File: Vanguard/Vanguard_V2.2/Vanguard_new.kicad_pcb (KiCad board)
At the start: 4 copper layers, 46.2 x 50.9 mm, 74 parts, among them J1 USB_C, J2 Conn_02x03_Pin, J3 Micro_SD_Card_Det1, J4 STARBOARD_SERVO, J5 PORTSIDE_SERVO, J6 Conn_01x02_Pin, Q1 BSS138, Q2 BSS138, Q3 BSS138, Q4 BSS138, U1 ATSAMD11D14A-M, U2 ATmega4809-A, U3 AT25DF641A-SH-T, U4 AP2112K-3.3, U5 MPM3610AGQV-P, U6 BNO086, U7 TXB0104D, U8 TPS61092, Y1 32.768kHz

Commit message: PCB
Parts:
- removed REF** (x3): MountingHole_2.2mm_M2, MountingHole:MountingHole_2.2mm_M2
- moved J3 310.8 mm to (424.9, 88.1), turned to 180 degrees
- moved D6 302.1 mm to (429.7, 64.5), turned to 90 degrees
- moved U5 300.3 mm to (428.0, 59.9)
- moved R14 300.0 mm to (423.9, 61.1), turned to 0 degrees
- moved C4 299.5 mm to (423.7, 60.2), turned to 180 degrees
- moved U7 299.1 mm to (425.1, 98.4), turned to 90 degrees
- moved J2 295.7 mm to (406.3, 71.4), turned to 180 degrees
- moved D1 294.8 mm to (398.5, 61.8), turned to 90 degrees
- moved J1 294.3 mm to (394.0, 62.0), turned to -90 degrees
- moved R15 294.0 mm to (427.0, 63.2)
- moved C5 292.4 mm to (427.2, 64.2), turned to 180 degrees
- moved R16 291.9 mm to (425.1, 63.2), turned to 180 degrees
- moved J5 290.2 mm to (398.9, 100.9), turned to -90 degrees
- moved R2 290.0 mm to (399.9, 65.2), turned to 180 degrees
- moved R1 289.8 mm to (396.0, 62.9)
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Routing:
- net RST: track 184.1 -> 40.0 mm, vias 13 -> 1
- net GND: track 88.2 -> 181.6 mm, vias 28 -> 19
- net VBUS_out: track 83.5 -> 16.7 mm, vias 6 -> 0
- net +5V: track 65.7 -> 16.0 mm, vias 2 -> 0
- net SDA: track 40.7 -> 10.2 mm, vias 3 -> 0
- net PORT_SERVO: track 27.5 -> 0.00 mm, vias 1 -> 0
- net STAR_SERVO: track 27.3 -> 0.00 mm, vias 1 -> 0
- net PA1/MOSI: track 20.8 -> 0.00 mm, vias 2 -> 0
- net PA2/SCK: track 19.1 -> 0.00 mm, vias 2 -> 0
- net UPDI: track 39.0 -> 20.7 mm, vias 4 -> 0
- net (no net): track 0.00 -> 17.3 mm
- net D7: track 16.1 -> 0.00 mm, vias 2 -> 0
- net D4: track 15.4 -> 0.00 mm, vias 2 -> 0
- net D6: track 15.0 -> 0.00 mm
- net Net-(J2-Pin_6): track 19.0 -> 4.00 mm, vias 3 -> 0
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- added copper zone on B.Cu, net (none)
- added copper zone on F.Cu, net (none)
- added copper zone on In1.Cu, net GND
- added copper zone on In2.Cu, net GND
- removed copper zone on B.Cu, net GND
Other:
- board size 46.2 x 50.9 mm -> 420.8 x 192.8 mm
- board text removed: "portside"
- board text removed: "starboard"

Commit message: started pcb
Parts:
- removed J1: USB_C, Connector_USB:USB_C_Plug_Molex_105444
- added J7: USB_B_Micro, Connector_USB:USB_Micro-B_Wuerth_614105150721_Vertical_CircularHoles, F.Cu at (108.3, 39.6)
- moved U7 398.0 mm to (35.6, 180.2), turned to 180 degrees
- moved J3 389.6 mm to (45.8, 178.2), turned to 90 degrees
- moved R22 373.4 mm to (25.6, 107.3)
- moved R23 371.4 mm to (29.2, 107.5), turned to 0 degrees
- moved R21 370.4 mm to (27.6, 107.3)
- moved Y1 370.3 mm to (26.6, 111.9), turned to -90 degrees
- moved C2 368.6 mm to (28.0, 110.7)
- moved ADR1 368.3 mm to (32.4, 106.7), turned to 180 degrees
- moved C3 368.1 mm to (28.0, 114.9), turned to -90 degrees
- moved U6 366.2 mm to (30.5, 111.7), turned to 90 degrees
- moved R20 366.1 mm to (33.7, 108.4), turned to 0 degrees
- moved R19 365.6 mm to (33.2, 110.0)
- moved R18 363.2 mm to (33.7, 111.5), turned to 0 degrees
- moved R24 362.9 mm to (30.8, 115.6), turned to 90 degrees
- moved C7 362.4 mm to (33.4, 112.5), turned to 0 degrees
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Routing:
- net GND: track 181.6 -> 6.33 mm, vias 19 -> 0
- net UPDI: track 20.7 -> 0.00 mm
- net RST: track 40.0 -> 19.7 mm, vias 1 -> 0
- net Net-(D1-I/O1): track 19.8 -> 0.00 mm
- net Net-(D1-I/O2): track 18.0 -> 0.00 mm, vias 2 -> 0
- net (no net): track 17.3 -> 0.00 mm
- net Net-(D2-K): track 17.0 -> 0.00 mm
- net Net-(D3-K): track 16.2 -> 0.00 mm
- net Net-(J2-Pin_2): track 13.4 -> 0.00 mm, vias 2 -> 0
- net RX0: track 12.5 -> 0.00 mm
- net TX0: track 12.4 -> 0.00 mm, vias 2 -> 0
- net SCL: track 12.0 -> 0.00 mm, vias 2 -> 0
- net +5V: track 16.0 -> 4.63 mm
- net Net-(J2-Pin_3): track 11.1 -> 0.00 mm
- net SDA: track 10.2 -> 0.00 mm
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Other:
- board size 420.8 x 192.8 mm -> 277.3 x 192.8 mm

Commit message: schematic + pcb changes
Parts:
- removed U5: MPM3610AGQV-P, MPM3610AGQV_P:CONV_MPM3620AGQV-P
- added U9: MPM3610AGQV-P, MPM3610AGQV_P:CONV_MPM3620AGQV-P, F.Cu at (278.9, 26.6)
- moved C5 78.7 mm to (282.3, 26.1), turned to 90 degrees
- moved C6 77.0 mm to (284.1, 26.7), turned to 180 degrees
- moved R15 45.3 mm to (281.4, 25.9), turned to 90 degrees
- moved D5 44.0 mm to (283.7, 24.9), turned to 180 degrees
- moved R17 33.9 mm to (283.9, 25.8), turned to 180 degrees
- moved R16 31.6 mm to (281.5, 24.0), turned to 90 degrees
- moved U4 3.32 mm to (283.2, 28.8)
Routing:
- net Net-(U9-FB): track 0.00 -> 11.1 mm
- net Net-(U4-EN): track 0.00 -> 7.61 mm
- net Net-(D5-A): track 0.00 -> 0.87 mm
- net RST: track 19.7 -> 20.6 mm

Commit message: pcb finished
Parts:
- removed J7: USB_B_Micro, Connector_USB:USB_Micro-B_Wuerth_614105150721_Vertical_CircularHoles
- removed R8: DNP, Resistor_SMD:R_0402_1005Metric
- added P1: USB_C_Plug_USB2.0, Connector_USB:USB_C_Plug_Molex_105444, F.Cu at (340.5, 83.7)
- moved U7 337.8 mm to (363.0, 97.1), turned to 90 degrees
- moved J3 326.9 mm to (365.0, 107.4), turned to 0 degrees
- moved R22 314.8 mm to (340.2, 94.7)
- moved C7 314.1 mm to (347.3, 100.0)
- moved ADR1 314.1 mm to (346.3, 94.0)
- moved C2 314.1 mm to (341.9, 98.1)
- moved C3 314.1 mm to (341.9, 102.2)
- moved R18 314.1 mm to (347.5, 98.8)
- moved R19 314.1 mm to (347.1, 97.3)
- moved R21 314.1 mm to (341.5, 94.6)
- moved Y1 314.1 mm to (340.5, 99.2)
- moved R20 314.1 mm to (347.5, 95.8)
- moved R23 314.1 mm to (343.1, 94.8)
- moved R24 314.1 mm to (344.6, 102.9)
- moved U6 314.1 mm to (344.4, 99.1)
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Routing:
- net RST: track 20.6 -> 194.7 mm, vias 0 -> 16
- net GND: track 6.33 -> 111.6 mm, vias 0 -> 25
- net +5V: track 4.63 -> 86.0 mm, vias 0 -> 1
- net VBUS_out: track 10.5 -> 76.9 mm, vias 0 -> 3
- net PORT_SERVO: track 0.00 -> 51.6 mm, vias 0 -> 1
- net PORT_BLUE: track 0.00 -> 50.4 mm, vias 0 -> 2
- net PORT_GREEN: track 0.00 -> 50.3 mm, vias 0 -> 2
- net PORT_RED: track 0.00 -> 49.1 mm, vias 0 -> 2
- net STAR_SERVO: track 0.00 -> 45.6 mm, vias 0 -> 1
- net SCL: track 0.00 -> 43.7 mm, vias 0 -> 2
- net UPDI: track 0.00 -> 40.2 mm, vias 0 -> 2
- net SDA: track 0.00 -> 35.5 mm, vias 0 -> 2
- net CD: track 0.00 -> 32.8 mm, vias 0 -> 2
- net STAR_BLUE: track 0.00 -> 31.9 mm
- net D4: track 0.00 -> 31.0 mm, vias 0 -> 4
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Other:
- board size 277.3 x 192.8 mm -> 377.4 x 192.8 mm
- board text added: "PCB Edge"

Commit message: pcb changes
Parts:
- moved C6 165.6 mm to (218.8, 91.5)
- moved C8 165.6 mm to (193.4, 93.0)
- moved D3 165.6 mm to (193.9, 106.4)
- moved D6 165.6 mm to (217.8, 101.2)
- moved R3 165.6 mm to (195.6, 106.4)
- moved R4 165.6 mm to (195.0, 97.5)
- moved STARBOARD_RGB1 165.6 mm to (220.0, 127.3)
- moved BZ1 165.6 mm to (218.3, 119.0)
- moved C10 165.6 mm to (202.7, 93.9)
- moved C2 165.6 mm to (177.0, 113.3)
- moved C3 165.6 mm to (177.0, 117.5)
- moved C4 165.6 mm to (214.9, 96.9)
- moved C5 165.6 mm to (218.2, 93.2)
- moved C7 165.6 mm to (182.4, 115.2)
- moved C9 165.6 mm to (203.5, 93.8)
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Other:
- board size 377.4 x 192.8 mm -> 50 x 40 mm

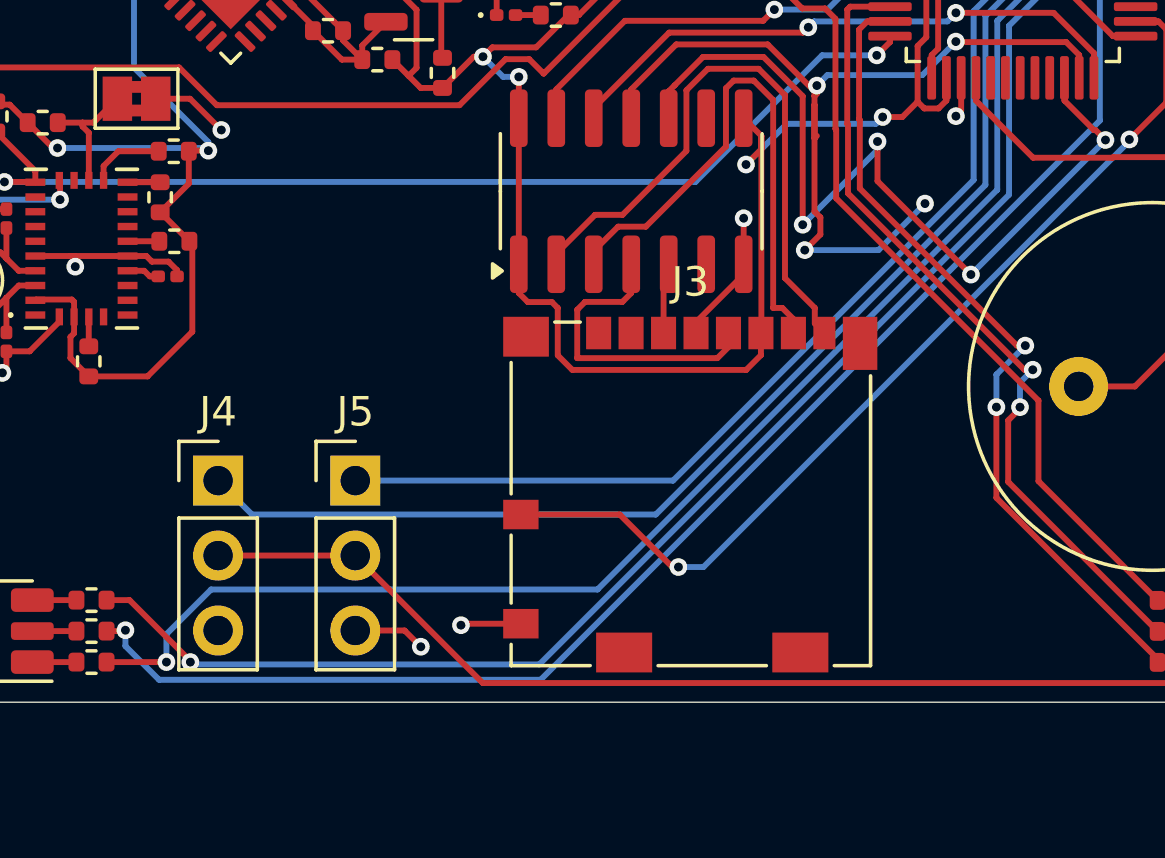
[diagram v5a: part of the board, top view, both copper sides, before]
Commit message: port side starboard servo port swap
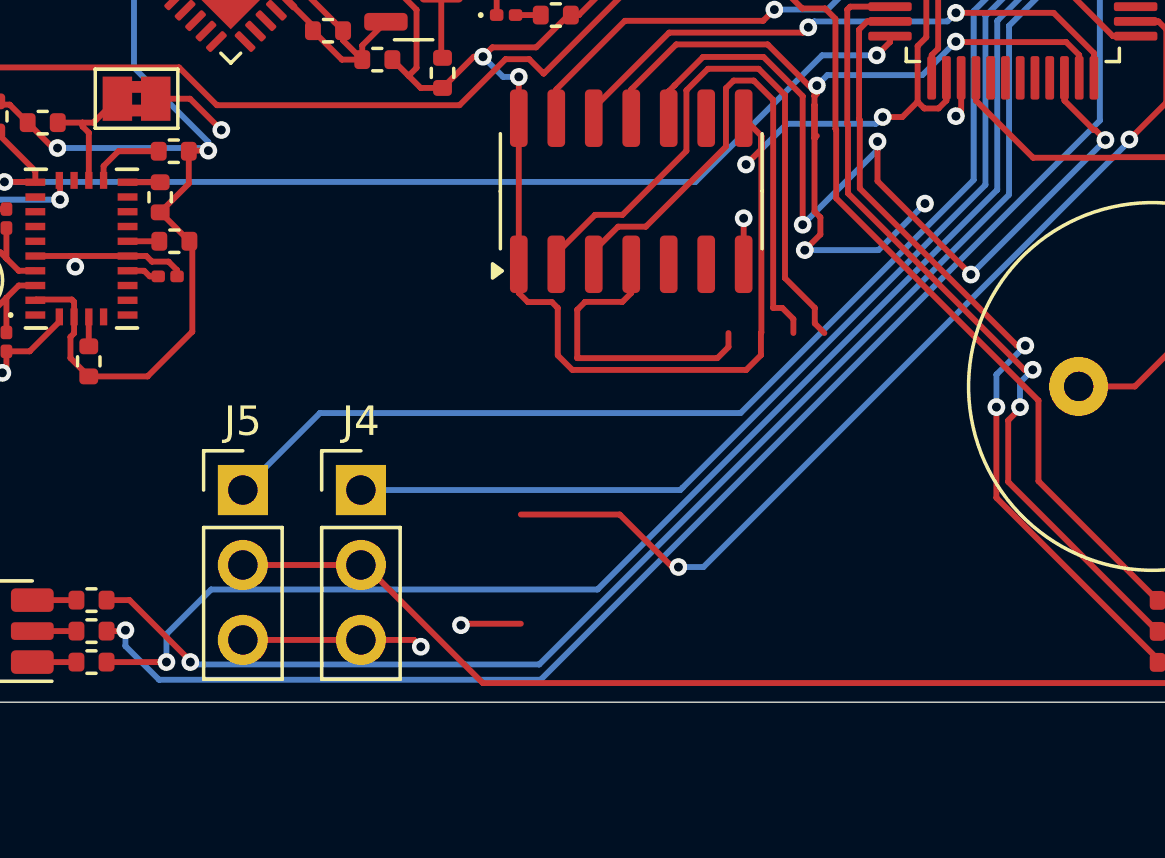
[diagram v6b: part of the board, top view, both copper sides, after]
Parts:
- removed J3: Micro_SD_Card_Det1, Connector_Card:microSD_HC_Molex_104031-0811
- moved J4 4.85 mm to (189.0, 122.5)
- moved J5 3.82 mm to (185.0, 122.5)
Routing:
- net STAR_SERVO: track 45.6 -> 40.0 mm
- net PORT_SERVO: track 51.6 -> 55.5 mm
- net Net-(J3-CMD): track 2.40 -> 0.25 mm
- net GND: track 111.6 -> 112.6 mm
- net +5V: track 86.0 -> 85.3 mm

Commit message: started wiring pcb
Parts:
- removed P1: USB_C_Plug_USB2.0, Connector_USB:USB_C_Plug_Molex_105444
- added J1: USB_C_Receptacle_USB2.0_16P, Connector_USB:USB_C_Receptacle_Amphenol_12401548E4-2A, F.Cu at (48.2, 24.9)
- added J3: Micro_SD_Card_Det1, Connector_Card:microSD_HC_Molex_104031-0811, F.Cu at (55.1, 158.9)
- added R31: 5k1, Resistor_SMD:R_0402_1005Metric, F.Cu at (70.8, 37.2)
- added R32: 5k1, Resistor_SMD:R_0402_1005Metric, F.Cu at (70.8, 39.2)
- added R8: DNP, Resistor_SMD:R_0402_1005Metric, F.Cu at (62.1, 33.3)
- added U5: BD1020HFV, Package_TO_SOT_SMD:HVSOF5, F.Cu at (75.7, 112.1)
- C10: value 100 uF -> 100u; footprint Capacitor_SMD:C_0201_0603Metric -> Capacitor_SMD:CP_Elec_6.3x5.4
- C2, C3: value 22pF -> 2p2
- C7: value 0.1uF -> 0u1F
- C8: value 10 uF -> 10u
- C9: value 2.2uF -> 2u2
- L1: value 6.8 uH -> 6u8
- R19, R20: value 4.7k -> 4k7
- R21, R22: value 2.2k -> 2k2
- U3: footprint AT25DF641A-SH-T:SOIC127P798X216-8N -> Package_SO:SOIC-8_3.9x4.9mm_P1.27mm
- U6: footprint BNO086:IC_BNO086 -> Package_LGA:LGA-28_5.2x3.8mm_P0.5mm
- U9: footprint MPM3610AGQV_P:CONV_MPM3620AGQV-P -> Package_DFN_QFN:QFN-16-1EP_3x3mm_P0.5mm_EP1.7x1.7mm
- moved U7 159.9 mm to (44.8, 157.6), turned to 0 degrees
- moved R3 152.9 mm to (59.2, 37.2), turned to 0 degrees
- moved R7 150.8 mm to (62.1, 31.3), turned to 0 degrees
- moved R10 148.4 mm to (62.1, 37.2), turned to 0 degrees
- moved R4 147.7 mm to (59.2, 39.2), turned to 0 degrees
- moved R13 147.6 mm to (62.1, 43.2)
- moved R6 145.5 mm to (59.2, 43.2), turned to 0 degrees
- moved R9 144.6 mm to (62.1, 35.3), turned to 0 degrees
- moved R5 144.5 mm to (59.2, 41.2)
- moved R12 143.8 mm to (62.1, 41.2)
- moved Q2 141.5 mm to (74.9, 32.6)
- moved R2 140.5 mm to (59.2, 35.3), turned to 0 degrees
- moved Q1 139.5 mm to (74.9, 28.0)
- moved R11 138.6 mm to (62.1, 39.2), turned to 0 degrees
- moved R1 137.3 mm to (59.2, 33.3)
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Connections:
- net RST renamed +3.3V
- C1 pad 1: VBUS_out -> Net-(D1-GND)
- C5 pad 1: Net-(U4-EN) -> Net-(D6-K)
- C8 pad 1: VBUS_out -> Net-(D1-GND)
- D1 pad 1: VBUS_out -> Net-(D1-GND)
- D1 pad 4: VBUS_out -> Net-(D1-GND)
- D6 pad 1: GND -> Net-(D6-K)
- D6 pad 2: VBUS_out -> Net-(D1-GND)
- J6 pad 1: VBUS_out -> Net-(D1-GND)
- L1 pad 1: VBUS_out -> Net-(D1-GND)
- Q1 pad 2: /RX_UPDI -> /TX_UPDI
- R1 pad 1: VBUS_out -> Net-(D1-GND)
- R15 pad 1: Net-(U4-EN) -> Net-(D6-K)
- R5 pad 2: /RX_UPDI -> /TX_UPDI
- R6 pad 2: /RX_UPDI -> /TX_UPDI
- U1 pad 11: /RX_UPDI -> /TX_UPDI
- U1 pad 15: Net-(D3-K) -> Net-(D2-K)
- U1 pad 16: Net-(D2-K) -> Net-(D3-K)
- U2 pad 3: unconnected-(U2-PA7-Pad3) -> TEMP_SENSOR
- U4 pad 1: Net-(U4-EN) -> Net-(D6-K)
- U4 pad 3: Net-(U4-EN) -> Net-(D6-K)
- U8 pad 11: VBUS_out -> Net-(D1-GND)
- U8 pad 8: VBUS_out -> Net-(D1-GND)
- U9 pad 2: VBUS_out -> unconnected-(U9-VCC-Pad2)
- U9 pad 4: Net-(U9-SW-Pad19) -> unconnected-(U9-SW-Pad19)_1
- U9 pad 5: Net-(U9-SW-Pad19) -> unconnected-(U9-SW-Pad19)_2
- U9 pad 6: Net-(U9-SW-Pad19) -> unconnected-(U9-SW-Pad19)
- U9 pad 7: Net-(U4-EN) -> Net-(D6-K)
- U9 pad 8: Net-(U4-EN) -> Net-(D6-K)
- U9 pad 9: Net-(U4-EN) -> Net-(D6-K)
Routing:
- net +3.3V: track 194.7 -> 17.3 mm, vias 16 -> 0
- net +5V: track 85.3 -> 0.00 mm, vias 1 -> 0
- net GND: track 112.6 -> 33.7 mm, vias 25 -> 0
- net VBUS_out: track 76.9 -> 0.00 mm, vias 3 -> 0
- net PORT_SERVO: track 55.5 -> 0.00 mm, vias 1 -> 0
- net PORT_BLUE: track 50.4 -> 0.00 mm, vias 2 -> 0
- net PORT_GREEN: track 50.3 -> 0.00 mm, vias 2 -> 0
- net PORT_RED: track 49.1 -> 0.00 mm, vias 2 -> 0
- net SCL: track 43.7 -> 0.00 mm, vias 2 -> 0
- net UPDI: track 40.2 -> 0.00 mm, vias 2 -> 0
- net STAR_SERVO: track 40.0 -> 0.00 mm, vias 1 -> 0
- net SDA: track 35.5 -> 0.00 mm, vias 2 -> 0
- net CD: track 32.8 -> 0.00 mm, vias 2 -> 0
- net STAR_BLUE: track 31.9 -> 0.00 mm
- net D4: track 31.0 -> 0.00 mm, vias 4 -> 0
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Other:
- board size 50 x 40 mm -> 273.2 x 187.6 mm

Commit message: finished wiring, no drc
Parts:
- removed R8: DNP, Resistor_SMD:R_0402_1005Metric
- moved U7 519.2 mm to (558.4, 81.3), turned to -90 degrees
- moved R23 508.3 mm to (562.8, 108.8), turned to 90 degrees
- moved ADR1 507.9 mm to (562.6, 106.2), turned to -90 degrees
- moved J3 506.5 mm to (557.0, 91.6), turned to 0 degrees
- moved R20 506.4 mm to (561.8, 108.8), turned to -90 degrees
- moved R19 505.2 mm to (561.2, 110.2), turned to 0 degrees
- moved R18 500.1 mm to (558.6, 110.6), turned to -90 degrees
- moved U6 499.4 mm to (558.4, 107.5), turned to 0 degrees
- moved Y1 499.1 mm to (558.3, 103.5), turned to 180 degrees
- moved C7 498.1 mm to (557.6, 110.4), turned to -90 degrees
- moved C2 498.1 mm to (557.8, 101.1), turned to 90 degrees
- moved C3 496.7 mm to (557.1, 101.1), turned to 90 degrees
- moved R24 491.6 mm to (554.5, 107.7), turned to 0 degrees
- moved R21 484.5 mm to (553.7, 105.5)
- moved R13 484.4 mm to (545.2, 78.5), turned to 90 degrees
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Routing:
- net +3.3V: track 17.3 -> 176.1 mm, vias 0 -> 14
- net GND: track 33.7 -> 152.7 mm, vias 0 -> 22
- net +5V: track 0.00 -> 49.0 mm, vias 0 -> 2
- net SCL: track 0.00 -> 40.8 mm, vias 0 -> 2
- net STAR_BLUE: track 0.00 -> 35.9 mm, vias 0 -> 2
- net Net-(D1-GND): track 0.00 -> 34.9 mm, vias 0 -> 2
- net D7: track 0.00 -> 34.3 mm, vias 0 -> 2
- net STAR_RED: track 0.00 -> 34.1 mm, vias 0 -> 2
- net STAR_GREEN: track 0.00 -> 34.0 mm, vias 0 -> 4
- net SDA: track 0.00 -> 33.2 mm
- net D6: track 0.00 -> 30.3 mm, vias 0 -> 2
- net D4: track 0.00 -> 30.0 mm, vias 0 -> 2
- net STAR_SERVO: track 0.00 -> 29.7 mm, vias 0 -> 2
- net TX0: track 0.00 -> 29.5 mm
- net PA3/SS: track 0.00 -> 28.7 mm, vias 0 -> 4
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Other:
- board size 273.2 x 187.6 mm -> 50 x 41.2 mm
